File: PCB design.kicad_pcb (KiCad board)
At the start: 2 copper layers, 19 parts, among them SW1 ACT4533AYH-T

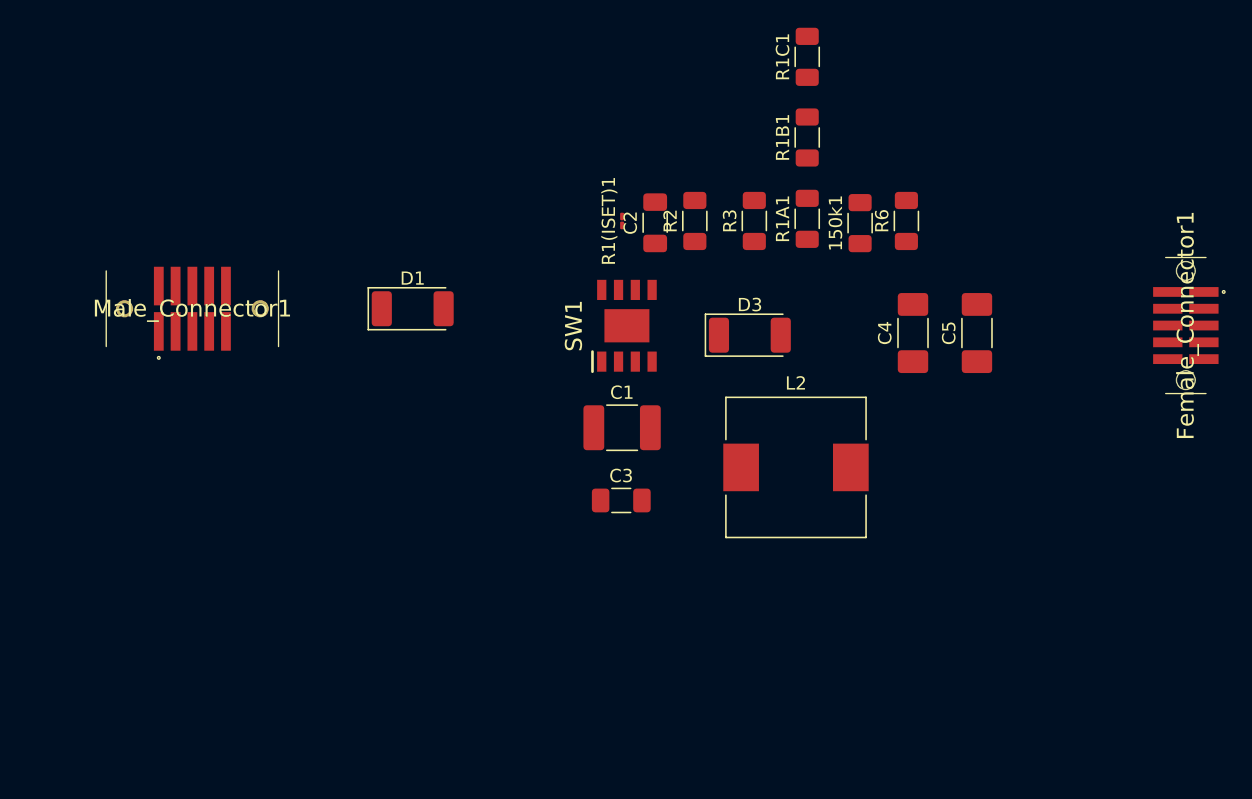
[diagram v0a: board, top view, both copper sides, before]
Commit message: Added all footprints to pcb design, something is fishy about the capasitors and resistances, we have too many resistors according to the datasheet and too few capasitors...
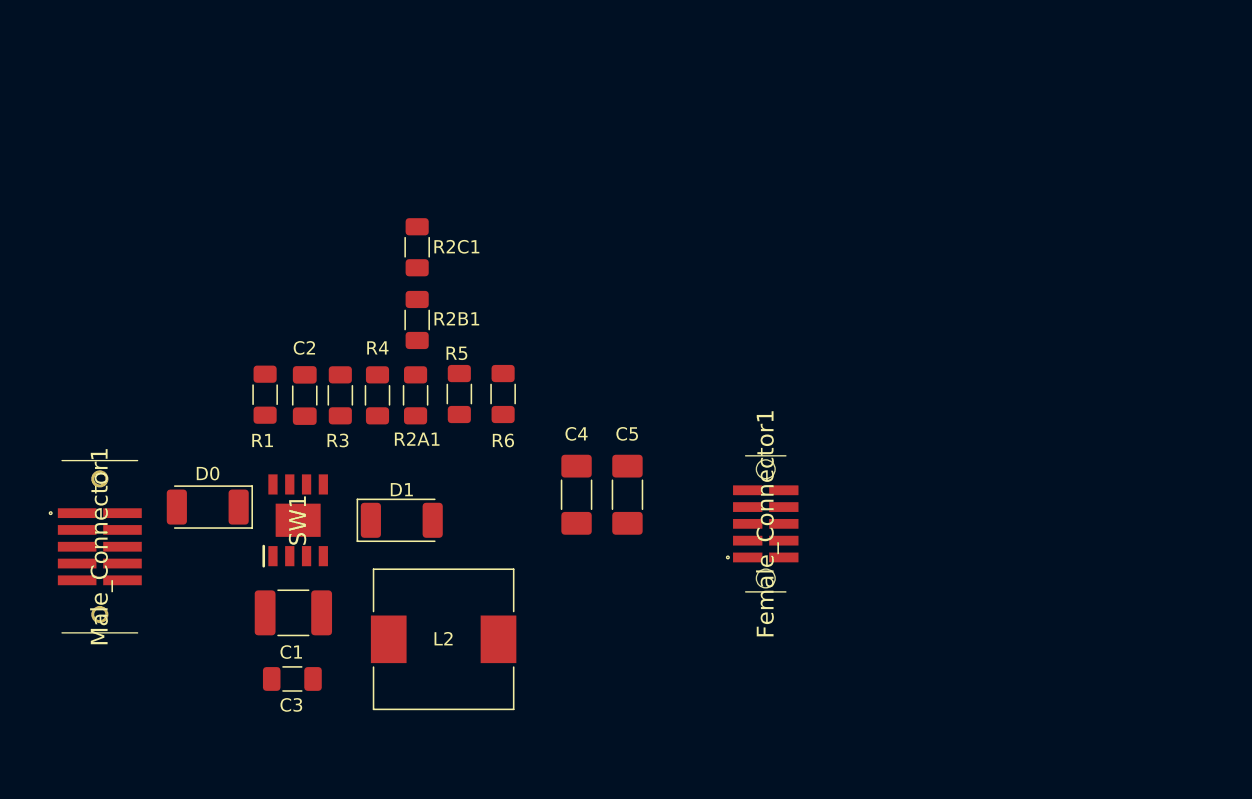
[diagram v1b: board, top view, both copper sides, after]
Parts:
- removed 150k1: R5, Resistor_SMD:R_1206_3216Metric_Pad1.30x1.75mm_HandSolder
- removed D3: SK54BLF_R1_00001, Diode_SMD:D_2010_5025Metric_Pad1.52x2.65mm_HandSolder
- removed R1(ISET)1: 25kΩ, Resistor_SMD:R_01005_0402Metric_Pad0.57x0.30mm_HandSolder
- removed R1A1, R1B1: 68kΩ, Resistor_SMD:R_1206_3216Metric_Pad1.30x1.75mm_HandSolder
- removed R1C1: 2.65kΩ, Resistor_SMD:R_1206_3216Metric_Pad1.30x1.75mm_HandSolder
- removed R2: 10kΩ, Resistor_SMD:R_1206_3216Metric_Pad1.30x1.75mm_HandSolder
- added D0: 0.7V, Diode_SMD:D_2010_5025Metric_Pad1.52x2.65mm_HandSolder, F.Cu at (109.2, 107.0)
- added R1: 25kΩ, Resistor_SMD:R_1206_3216Metric_Pad1.30x1.75mm_HandSolder, F.Cu at (113.5, 98.5)
- added R2A1: 2.65kΩ, Resistor_SMD:R_1206_3216Metric_Pad1.30x1.75mm_HandSolder, F.Cu at (124.9, 98.5)
- added R2B1: 68kΩ, Resistor_SMD:R_1206_3216Metric_Pad1.30x1.75mm_HandSolder, F.Cu at (125.0, 92.8)
- added R2C1: 68kΩ, Resistor_SMD:R_1206_3216Metric_Pad1.30x1.75mm_HandSolder, F.Cu at (125.0, 87.3)
- added R4: 10kΩ, Resistor_SMD:R_1206_3216Metric_Pad1.30x1.75mm_HandSolder, F.Cu at (122.0, 98.5)
- added R5: 150kΩ, Resistor_SMD:R_1206_3216Metric_Pad1.30x1.75mm_HandSolder, F.Cu at (128.2, 98.5)
- C1: value 22nF -> 22µF
- D1: value 0.7V -> 40V/5A
- moved Female_Connector1 35.1 mm to (151.4, 108.3), turned to -90 degrees
- moved R3 34.0 mm to (119.2, 98.5)
- moved R6 33.2 mm to (131.5, 98.5)
- moved C5 32.7 mm to (137.1, 106.1), turned to -90 degrees
- moved L2 29.7 mm to (127.0, 117.0)
- moved C2 29.5 mm to (116.5, 98.6)
- moved SW1 28.9 mm to (116.0, 108.0)
- moved C1 28.5 mm to (115.6, 115.0), turned to 180 degrees
- moved C3 28.3 mm to (115.6, 120.0)
- moved C4 24.8 mm to (140.9, 106.1)
- moved Male_Connector1 19.3 mm to (101.0, 110.0), turned to -90 degrees
- moved D1 16.0 mm to (123.8, 108.0)
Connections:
- C1 pad 1: Net-(C1-+) -> GND
- C1 pad 2: Net-(C1--) -> PDU
- C3 pad 1: Net-(C1-+) -> Net-(D1-K)
- C4 pad 2: PDU -> GND
- C5 pad 1: PDU -> GND
- D1 pad 1: PDU -> Net-(D1-K)
- D1 pad 2: Net-(D1-A) -> GND
- Female_Connector1 pad 1: PDU -> GND
- L2 pad 1: Net-(C1-+) -> Net-(D1-K)
- Male_Connector1 pad 1: PDU -> GND
- R3 pad 2: PDU -> GND
- R6 pad 1: PDU -> GND
- SW1 pad 2: Net-(D1-A) -> Net-(D0-K)
- SW1 pad 3: Net-(C1--) -> Net-(D1-K)
- SW1 pad 4: PDU -> GND

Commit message: Added copper tracks: note not filled. Still not fixed issue with resistors and capasitors
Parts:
- turned D1 to 180 degrees
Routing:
- net GND: track 0.00 -> 107.3 mm
- net +12V: track 0.00 -> 95.1 mm
- net Net-(D1-K): track 0.00 -> 61.7 mm
- net (no net): track 0.00 -> 32.9 mm
- net Net-(SW1-FB): track 0.00 -> 22.2 mm
- net PDU: track 0.00 -> 19.3 mm
- net Net-(D0-K): track 0.00 -> 10.5 mm
- net Net-(SW1-ISET): track 0.00 -> 5.78 mm
- net Net-(C2-Pad1): track 0.00 -> 3.47 mm
- net Net-(R2B1-Pad1): track 0.00 -> 2.15 mm
- net Net-(R2A1-Pad1): track 0.00 -> 2.15 mm

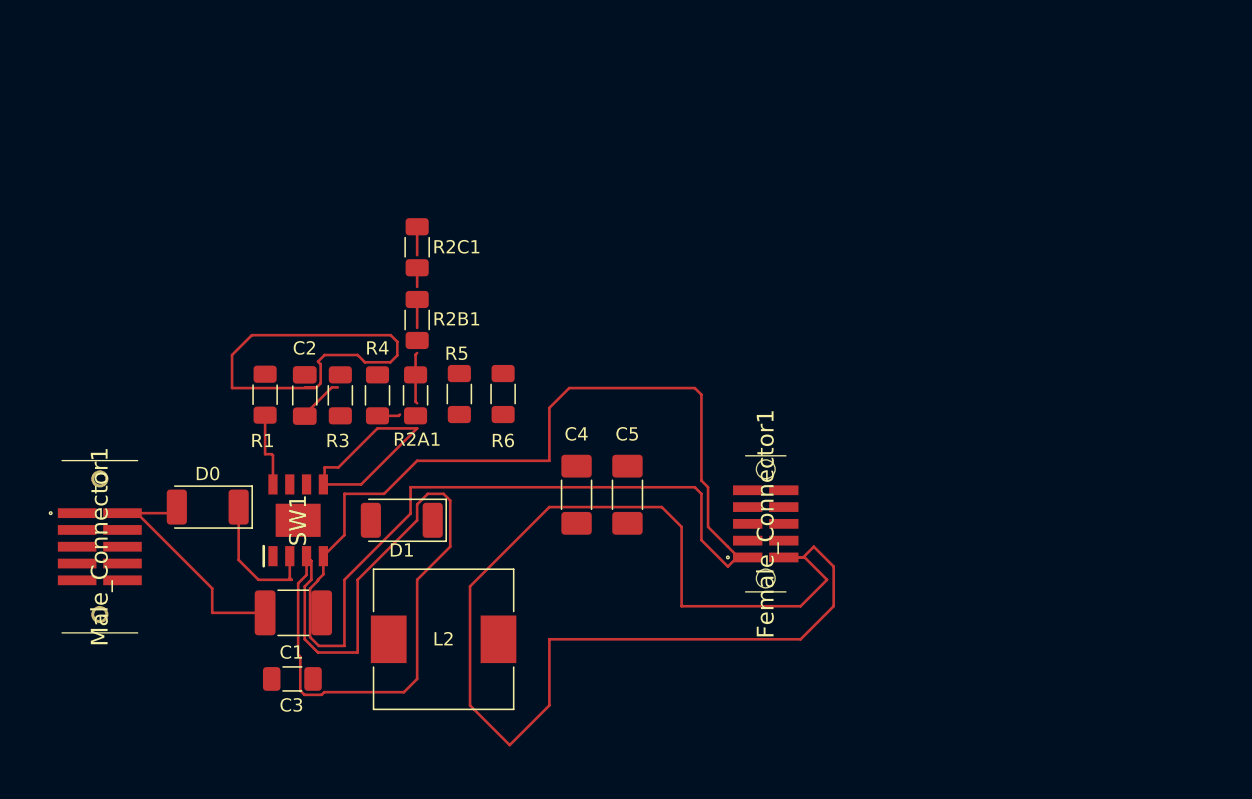
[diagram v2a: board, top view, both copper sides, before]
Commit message: Finished the ground layer and wiring of all components in PCB design. Ready for evaluation.
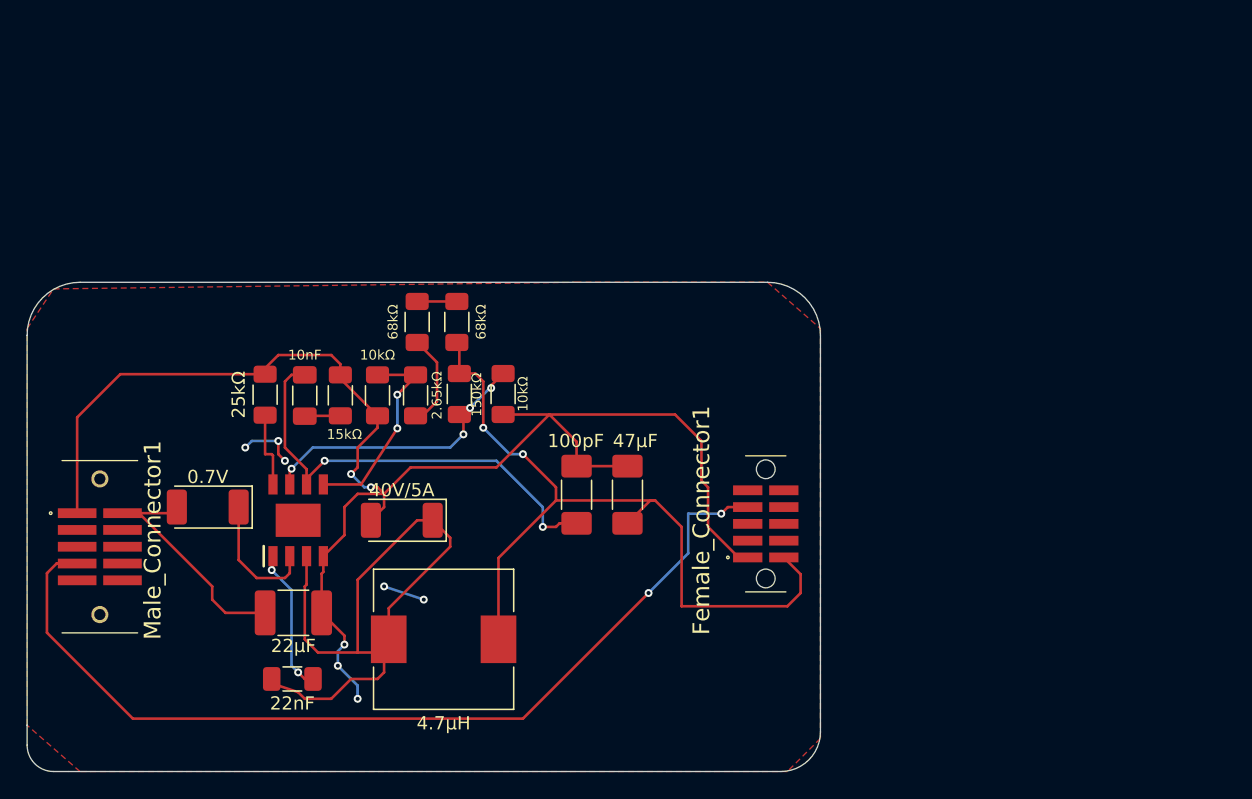
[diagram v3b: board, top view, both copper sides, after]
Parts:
- L2: value LB3218T102K -> 4.7µH
- moved R2C1 6.40 mm to (128.0, 93.0)
- moved R2B1 0.15 mm to (125.0, 93.0), turned to -90 degrees
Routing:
- net I/O: track 0.00 -> 71.2 mm, vias 0 -> 2
- net +12V: track 95.1 -> 60.4 mm, vias 0 -> 2
- net Net-(C5--): track 0.00 -> 34.6 mm, vias 0 -> 2
- net (no net): track 32.9 -> 0.00 mm
- net Net-(SW1-EN/OVP): track 0.00 -> 21.7 mm, vias 0 -> 4
- net Net-(D1-K): track 61.7 -> 48.2 mm
- net GND: track 107.3 -> 120.3 mm, vias 0 -> 10
- net Net-(SW1-HSB): track 0.00 -> 11.0 mm, vias 0 -> 2
- net Net-(SW1-FB): track 22.2 -> 15.4 mm, vias 0 -> 2
- net Net-(R2A1-Pad1): track 2.15 -> 7.15 mm
- net Net-(R2B1-Pad1): track 2.15 -> 3.00 mm
- net Net-(C2-Pad1): track 3.47 -> 2.83 mm
- net Net-(D0-K): track 10.5 -> 9.87 mm
- added copper zone on F.Cu, net GND
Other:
- board outline added: 60 x 37 mm
